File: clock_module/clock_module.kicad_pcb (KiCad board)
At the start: 2 copper layers, 100 x 100 mm, 19 parts, among them SW1 SW_SPST, SW2 SW_Push, SW3 SW_SPDT, SW4 SW_SPDT, U1 74HC14

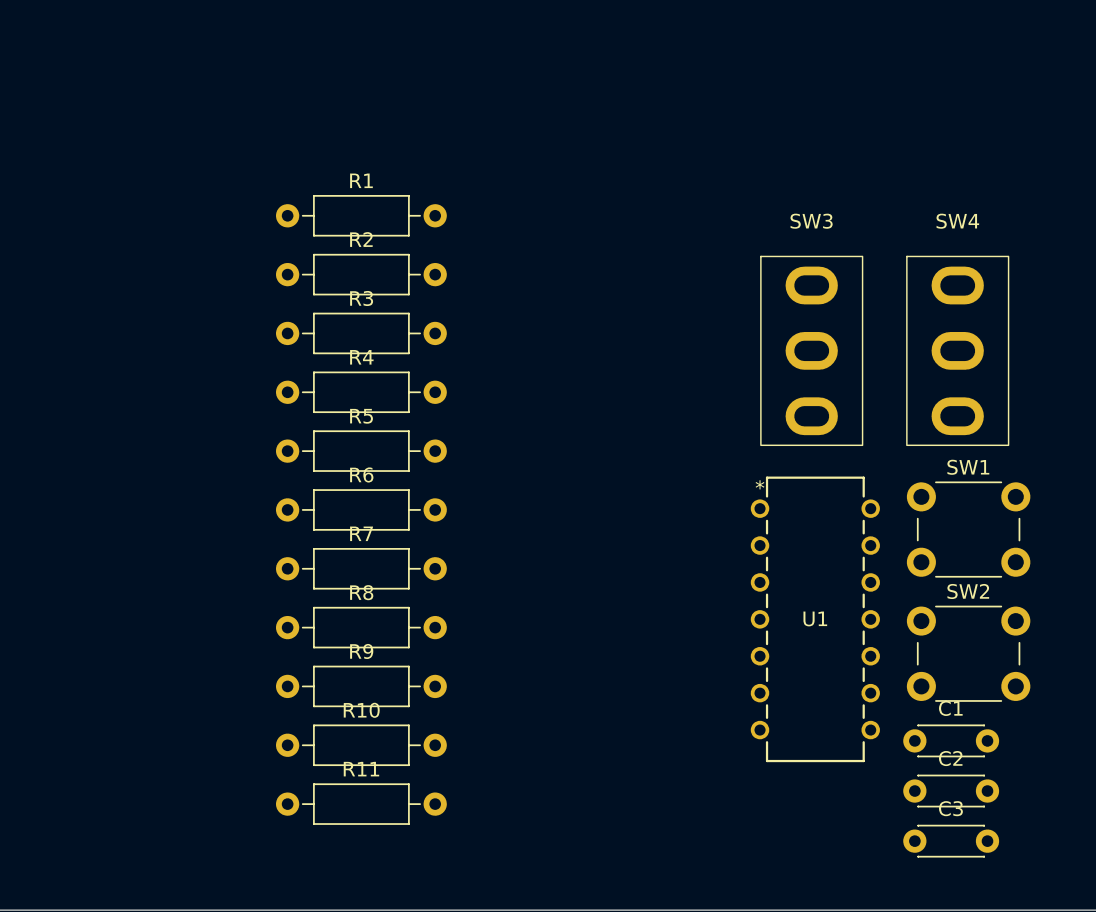
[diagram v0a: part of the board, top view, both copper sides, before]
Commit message: フットプリント追加
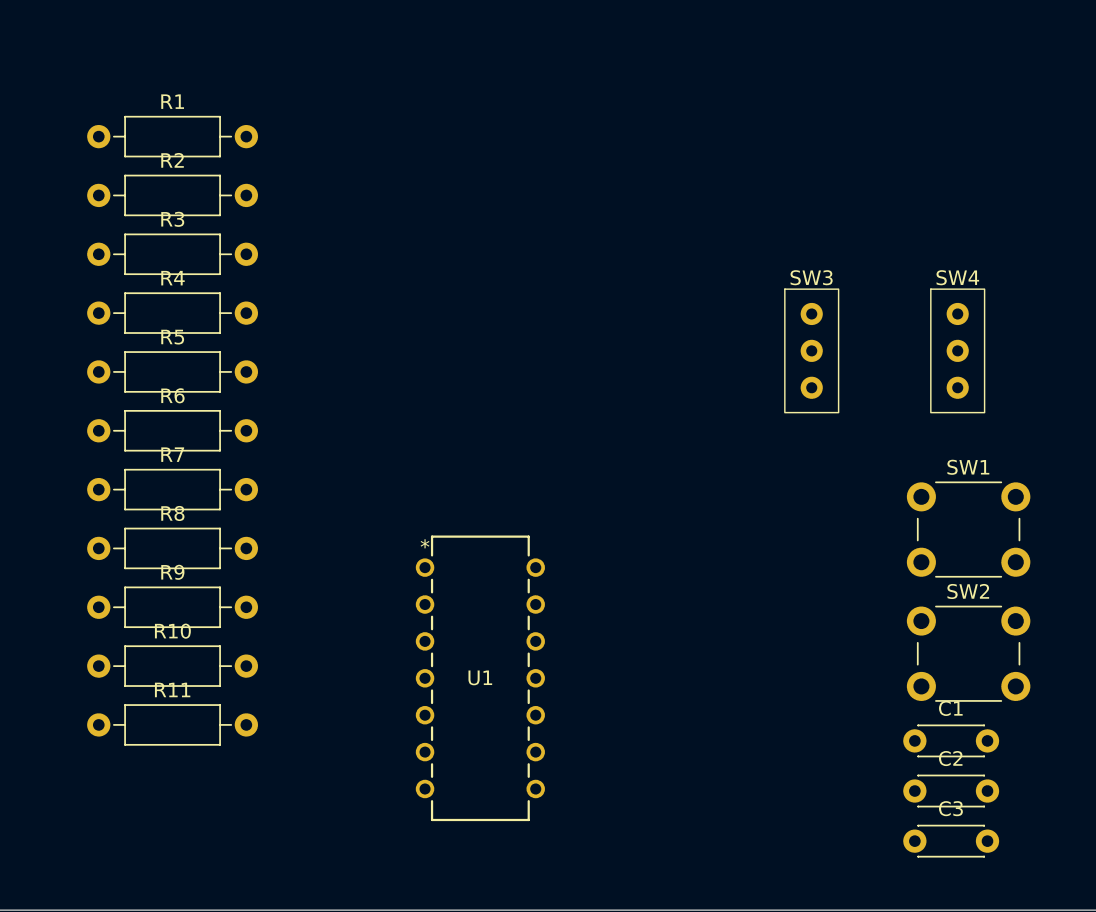
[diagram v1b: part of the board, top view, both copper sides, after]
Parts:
- SW3, SW4: footprint footprint_library:SPDT -> footprint_library:SS-12D00G3
- moved U1 23.4 mm to (136.4, 126.4)
- moved R10 14.1 mm to (113.9, 133.2)
- moved R8 14.1 mm to (113.9, 125.1)
- moved R1 14.1 mm to (113.9, 96.8)
- moved R2 14.1 mm to (113.9, 100.8)
- moved R3 14.1 mm to (113.9, 104.8)
- moved R5 14.1 mm to (113.9, 113.0)
- moved R6 14.1 mm to (113.9, 117.0)
- moved R7 14.1 mm to (113.9, 121.0)
- moved R11 14.1 mm to (113.9, 137.2)
- moved R4 14.1 mm to (113.9, 108.9)
- moved R9 14.1 mm to (113.9, 129.2)
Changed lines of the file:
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@@
 	(footprint "Resistor_THT:R_Axial_DIN0207_L6.3mm_D2.5mm_P10.16mm_Horizontal"
 		(layer "F.Cu")
-		(at 126.92 102.2)
+		(at 113.92 96.75)
 		(descr "Resistor, Axial_DIN0207 series, Axial, Horizontal, pin pitch=10.16mm, 0.25W = 1/4W, length*diameter=6.3*2.5mm^2, http://cdn-reichelt.de/documents/datenblatt/B400/1_4W%23YAG.pdf")
 		(tags "Resistor Axial_DIN0207 series Axial Horizontal pin pitch 10.16mm 0.25W = 1/4W length 6.3mm diameter 2.5mm")
@@
 	(footprint "Resistor_THT:R_Axial_DIN0207_L6.3mm_D2.5mm_P10.16mm_Horizontal"
 		(layer "F.Cu")
-		(at 126.92 122.45)
+		(at 113.92 117)
 		(descr "Resistor, Axial_DIN0207 series, Axial, Horizontal, pin pitch=10.16mm, 0.25W = 1/4W, length*diameter=6.3*2.5mm^2, http://cdn-reichelt.de/documents/datenblatt/B400/1_4W%23YAG.pdf")
 		(tags "Resistor Axial_DIN0207 series Axial Horizontal pin pitch 10.16mm 0.25W = 1/4W length 6.3mm diameter 2.5mm")
@@
 	(footprint "Resistor_THT:R_Axial_DIN0207_L6.3mm_D2.5mm_P10.16mm_Horizontal"
 		(layer "F.Cu")
-		(at 126.92 110.3)
+		(at 113.92 104.85)
 		(descr "Resistor, Axial_DIN0207 series, Axial, Horizontal, pin pitch=10.16mm, 0.25W = 1/4W, length*diameter=6.3*2.5mm^2, http://cdn-reichelt.de/documents/datenblatt/B400/1_4W%23YAG.pdf")
 		(tags "Resistor Axial_DIN0207 series Axial Horizontal pin pitch 10.16mm 0.25W = 1/4W length 6.3mm diameter 2.5mm")
@@
 		)
 	)
-	(footprint "footprint_library:SPDT"
+	(footprint "footprint_library:SS-12D00G3"
 		(layer "F.Cu")
 		(at 173.05 111.5)
 		(property "Reference" "SW4"
-			(at 0 -8.89 0)
+			(at 0 -5 0)
 			(unlocked yes)
 			(layer "F.SilkS")
@@
 		)
 		(property "Value" "SW_SPDT"
-			(at 0 -7.62 0)
+			(at 0 1 0)
 			(unlocked yes)
 			(layer "F.Fab")
@@
 			)
 		)
-		(property "Footprint" "footprint_library:SPDT"
+		(property "Footprint" "footprint_library:SS-12D00G3"
 			(at 0 0 0)
+			(unlocked yes)
 			(layer "F.Fab")
 			(hide yes)
 			(effects
 				(font
-					(size 1.27 1.27)
+					(size 1 1)
 					(thickness 0.15)
 				)
@@
 		(property "Datasheet" ""
 			(at 0 0 0)
+			(unlocked yes)
 			(layer "F.Fab")
 			(hide yes)
 			(effects
 				(font
-					(size 1.27 1.27)
+					(size 1 1)
 					(thickness 0.15)
 				)
@@
 		(property "Description" "Switch, single pole double throw"
 			(at 0 0 0)
+			(unlocked yes)
 			(layer "F.Fab")
 			(hide yes)
 			(effects
 				(font
-					(size 1.27 1.27)
+					(size 1 1)
 					(thickness 0.15)
 				)
@@
 		(attr through_hole)
 		(fp_rect
-			(start -3.5 -6.5)
-			(end 3.5 6.5)
+			(start -1.85 -4.25)
+			(end 1.85 4.25)
 			(stroke
 				(width 0.1)
@@
 		)
 		(fp_rect
-			(start -4.5 -7.5)
-			(end 4.5 7.5)
+			(start -2.54 -5.08)
+			(end 2.54 5.08)
 			(stroke
 				(width 0.05)
@@
 		)
 		(fp_text user "${REFERENCE}"
-			(at 0 -1.31 0)
+			(at 0 2.5 0)
 			(unlocked yes)
 			(layer "F.Fab")
@@
 			)
 		)
-		(pad "1" thru_hole oval
-			(at 0 -4.5)
-			(size 3.6 2.6)
-			(drill oval 2.4 1.4)
+		(pad "1" thru_hole circle
+			(at 0 -2.54)
+			(size 1.524 1.524)
+			(drill 0.762)
 			(layers "*.Cu" "*.Mask")
 			(remove_unused_layers no)
@@
 			(pintype "passive")
 		)
-		(pad "2" thru_hole oval
+		(pad "2" thru_hole circle
 			(at 0 0)
-			(size 3.6 2.6)
-			(drill oval 2.4 1.4)
+			(size 1.524 1.524)
+			(drill 0.762)
 			(layers "*.Cu" "*.Mask")
 			(remove_unused_layers no)
@@
 			(pintype "passive")
 		)
-		(pad "3" thru_hole oval
-			(at 0 4.5)
-			(size 3.6 2.6)
-			(drill oval 2.4 1.4)
+		(pad "3" thru_hole circle
+			(at 0 2.54)
+			(size 1.524 1.524)
+			(drill 0.762)
 			(layers "*.Cu" "*.Mask")
 			(remove_unused_layers no)
@@
 	(footprint "Resistor_THT:R_Axial_DIN0207_L6.3mm_D2.5mm_P10.16mm_Horizontal"
 		(layer "F.Cu")
-		(at 126.92 134.6)
+		(at 113.92 129.15)
 		(descr "Resistor, Axial_DIN0207 series, Axial, Horizontal, pin pitch=10.16mm, 0.25W = 1/4W, length*diameter=6.3*2.5mm^2, http://cdn-reichelt.de/documents/datenblatt/B400/1_4W%23YAG.pdf")
 		(tags "Resistor Axial_DIN0207 series Axial Horizontal pin pitch 10.16mm 0.25W = 1/4W length 6.3mm diameter 2.5mm")
@@
 	(footprint "Resistor_THT:R_Axial_DIN0207_L6.3mm_D2.5mm_P10.16mm_Horizontal"
 		(layer "F.Cu")
-		(at 126.92 118.4)
+		(at 113.92 112.95)
 		(descr "Resistor, Axial_DIN0207 series, Axial, Horizontal, pin pitch=10.16mm, 0.25W = 1/4W, length*diameter=6.3*2.5mm^2, http://cdn-reichelt.de/documents/datenblatt/B400/1_4W%23YAG.pdf")
 		(tags "Resistor Axial_DIN0207 series Axial Horizontal pin pitch 10.16mm 0.25W = 1/4W length 6.3mm diameter 2.5mm")
@@
 	(footprint "Resistor_THT:R_Axial_DIN0207_L6.3mm_D2.5mm_P10.16mm_Horizontal"
 		(layer "F.Cu")
-		(at 126.92 138.65)
+		(at 113.92 133.2)
 		(descr "Resistor, Axial_DIN0207 series, Axial, Horizontal, pin pitch=10.16mm, 0.25W = 1/4W, length*diameter=6.3*2.5mm^2, http://cdn-reichelt.de/documents/datenblatt/B400/1_4W%23YAG.pdf")
 		(tags "Resistor Axial_DIN0207 series Axial Horizontal pin pitch 10.16mm 0.25W = 1/4W length 6.3mm diameter 2.5mm")
@@
 	(footprint "footprint_library:DIP14_TOS"
 		(layer "F.Cu")
-		(at 159.4402 122.3618)
+		(at 136.38 126.42)
 		(tags "tc74hc14apf ")
 		(property "Reference" "U1"
@@
 	(footprint "Resistor_THT:R_Axial_DIN0207_L6.3mm_D2.5mm_P10.16mm_Horizontal"
 		(layer "F.Cu")
-		(at 126.92 142.7)
+		(at 113.92 137.25)
 		(descr "Resistor, Axial_DIN0207 series, Axial, Horizontal, pin pitch=10.16mm, 0.25W = 1/4W, length*diameter=6.3*2.5mm^2, http://cdn-reichelt.de/documents/datenblatt/B400/1_4W%23YAG.pdf")
 		(tags "Resistor Axial_DIN0207 series Axial Horizontal pin pitch 10.16mm 0.25W = 1/4W length 6.3mm diameter 2.5mm")
@@
 	(footprint "Resistor_THT:R_Axial_DIN0207_L6.3mm_D2.5mm_P10.16mm_Horizontal"
 		(layer "F.Cu")
-		(at 126.92 106.25)
+		(at 113.92 100.8)
 		(descr "Resistor, Axial_DIN0207 series, Axial, Horizontal, pin pitch=10.16mm, 0.25W = 1/4W, length*diameter=6.3*2.5mm^2, http://cdn-reichelt.de/documents/datenblatt/B400/1_4W%23YAG.pdf")
 		(tags "Resistor Axial_DIN0207 series Axial Horizontal pin pitch 10.16mm 0.25W = 1/4W length 6.3mm diameter 2.5mm")
@@
 	(footprint "Resistor_THT:R_Axial_DIN0207_L6.3mm_D2.5mm_P10.16mm_Horizontal"
 		(layer "F.Cu")
-		(at 126.92 130.55)
+		(at 113.92 125.1)
 		(descr "Resistor, Axial_DIN0207 series, Axial, Horizontal, pin pitch=10.16mm, 0.25W = 1/4W, length*diameter=6.3*2.5mm^2, http://cdn-reichelt.de/documents/datenblatt/B400/1_4W%23YAG.pdf")
 		(tags "Resistor Axial_DIN0207 series Axial Horizontal pin pitch 10.16mm 0.25W = 1/4W length 6.3mm diameter 2.5mm")
@@
 		)
 	)
-	(footprint "footprint_library:SPDT"
+	(footprint "footprint_library:SS-12D00G3"
 		(layer "F.Cu")
 		(at 163 111.5)
 		(property "Reference" "SW3"
-			(at 0 -8.89 0)
+			(at 0 -5 0)
 			(unlocked yes)
 			(layer "F.SilkS")
@@
 		)
 		(property "Value" "SW_SPDT"
-			(at 0 -7.62 0)
+			(at 0 1 0)
 			(unlocked yes)
 			(layer "F.Fab")
@@
 			)
 		)
-		(property "Footprint" "footprint_library:SPDT"
+		(property "Footprint" "footprint_library:SS-12D00G3"
 			(at 0 0 0)
+			(unlocked yes)
 			(layer "F.Fab")
 			(hide yes)
 			(effects
 				(font
-					(size 1.27 1.27)
+					(size 1 1)
 					(thickness 0.15)
 				)
@@
 		(property "Datasheet" ""
 			(at 0 0 0)
+			(unlocked yes)
 			(layer "F.Fab")
 			(hide yes)
 			(effects
 				(font
-					(size 1.27 1.27)
+					(size 1 1)
 					(thickness 0.15)
 				)
@@
 		(property "Description" "Switch, single pole double throw"
 			(at 0 0 0)
+			(unlocked yes)
 			(layer "F.Fab")
 			(hide yes)
 			(effects
 				(font
-					(size 1.27 1.27)
+					(size 1 1)
 					(thickness 0.15)
 				)
@@
 		(attr through_hole)
 		(fp_rect
-			(start -3.5 -6.5)
-			(end 3.5 6.5)
+			(start -1.85 -4.25)
+			(end 1.85 4.25)
 			(stroke
 				(width 0.1)
@@
 		)
 		(fp_rect
-			(start -4.5 -7.5)
-			(end 4.5 7.5)
+			(start -2.54 -5.08)
+			(end 2.54 5.08)
 			(stroke
 				(width 0.05)
@@
 		)
 		(fp_text user "${REFERENCE}"
-			(at 0 -1.31 0)
+			(at 0 2.5 0)
 			(unlocked yes)
 			(layer "F.Fab")
@@
 			)
 		)
-		(pad "1" thru_hole oval
-			(at 0 -4.5)
-			(size 3.6 2.6)
-			(drill oval 2.4 1.4)
+		(pad "1" thru_hole circle
+			(at 0 -2.54)
+			(size 1.524 1.524)
+			(drill 0.762)
 			(layers "*.Cu" "*.Mask")
 			(remove_unused_layers no)
@@
 			(pintype "passive")
 		)
-		(pad "2" thru_hole oval
+		(pad "2" thru_hole circle
 			(at 0 0)
-			(size 3.6 2.6)
-			(drill oval 2.4 1.4)
+			(size 1.524 1.524)
+			(drill 0.762)
 			(layers "*.Cu" "*.Mask")
 			(remove_unused_layers no)
@@
 			(pintype "passive")
 		)
-		(pad "3" thru_hole oval
-			(at 0 4.5)
-			(size 3.6 2.6)
-			(drill oval 2.4 1.4)
+		(pad "3" thru_hole circle
+			(at 0 2.54)
+			(size 1.524 1.524)
+			(drill 0.762)
 			(layers "*.Cu" "*.Mask")
 			(remove_unused_layers no)
@@
 	(footprint "Resistor_THT:R_Axial_DIN0207_L6.3mm_D2.5mm_P10.16mm_Horizontal"
 		(layer "F.Cu")
-		(at 126.92 126.5)
+		(at 113.92 121.05)
 		(descr "Resistor, Axial_DIN0207 series, Axial, Horizontal, pin pitch=10.16mm, 0.25W = 1/4W, length*diameter=6.3*2.5mm^2, http://cdn-reichelt.de/documents/datenblatt/B400/1_4W%23YAG.pdf")
 		(tags "Resistor Axial_DIN0207 series Axial Horizontal pin pitch 10.16mm 0.25W = 1/4W length 6.3mm diameter 2.5mm")
@@
 	(footprint "Resistor_THT:R_Axial_DIN0207_L6.3mm_D2.5mm_P10.16mm_Horizontal"
 		(layer "F.Cu")
-		(at 126.92 114.35)
+		(at 113.92 108.9)
 		(descr "Resistor, Axial_DIN0207 series, Axial, Horizontal, pin pitch=10.16mm, 0.25W = 1/4W, length*diameter=6.3*2.5mm^2, http://cdn-reichelt.de/documents/datenblatt/B400/1_4W%23YAG.pdf")
 		(tags "Resistor Axial_DIN0207 series Axial Horizontal pin pitch 10.16mm 0.25W = 1/4W length 6.3mm diameter 2.5mm")

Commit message: 電源回路wip
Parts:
- added C1: 100uF, Capacitor_THT:C_Disc_D4.3mm_W1.9mm_P5.00mm, F.Cu at (130.8, 78.1)
- added C10: 0.1uF, Capacitor_THT:C_Disc_D4.3mm_W1.9mm_P5.00mm, F.Cu at (139.7, 85.7)
- added C11: 0.1uF, Capacitor_THT:C_Disc_D4.3mm_W1.9mm_P5.00mm, F.Cu at (144.1, 85.7)
- added C12: 0.1uF, Capacitor_THT:C_Disc_D4.3mm_W1.9mm_P5.00mm, F.Cu at (148.6, 85.7)
- added C13: 0.1uF, Capacitor_THT:C_Disc_D4.3mm_W1.9mm_P5.00mm, F.Cu at (153.0, 85.7)
- added C14: 0.1uF, Capacitor_THT:C_Disc_D4.3mm_W1.9mm_P5.00mm, F.Cu at (157.5, 85.7)
- added C2: 0.1uF, Capacitor_THT:C_Disc_D4.3mm_W1.9mm_P5.00mm, F.Cu at (135.3, 78.1)
- added C3: 0.1uF, Capacitor_THT:C_Disc_D4.3mm_W1.9mm_P5.00mm, F.Cu at (139.7, 78.1)
- added C4: 0.1uF, Capacitor_THT:C_Disc_D4.3mm_W1.9mm_P5.00mm, F.Cu at (144.1, 78.1)
- added C5: 0.1uF, Capacitor_THT:C_Disc_D4.3mm_W1.9mm_P5.00mm, F.Cu at (148.6, 78.1)
- added C6: 0.1uF, Capacitor_THT:C_Disc_D4.3mm_W1.9mm_P5.00mm, F.Cu at (153.0, 78.1)
- added C7: 0.1uF, Capacitor_THT:C_Disc_D4.3mm_W1.9mm_P5.00mm, F.Cu at (157.5, 78.1)
- added C8: 0.1uF, Capacitor_THT:C_Disc_D4.3mm_W1.9mm_P5.00mm, F.Cu at (130.8, 85.7)
- added C9: 0.1uF, Capacitor_THT:C_Disc_D4.3mm_W1.9mm_P5.00mm, F.Cu at (135.3, 85.7)
- added J1: USB_C_Receptacle_PowerOnly_6P, footprint_library:UJC-HP-3-SMT-TR, F.Cu at (103.5, 77.2)
- added J2: Conn_01x02_Socket, Connector_PinSocket_2.54mm:PinSocket_1x02_P2.54mm_Horizontal, F.Cu at (188.6, 73.7)
- added R1: 1K, Resistor_THT:R_Axial_DIN0207_L6.3mm_D2.5mm_P10.16mm_Horizontal, F.Cu at (124.5, 83.2)
- added R2: 5.1K, Resistor_THT:R_Axial_DIN0207_L6.3mm_D2.5mm_P10.16mm_Horizontal, F.Cu at (114.3, 83.2)
- added R3: 5.1K, Resistor_THT:R_Axial_DIN0207_L6.3mm_D2.5mm_P10.16mm_Horizontal, F.Cu at (119.4, 83.2)
- moved SW1 34.7 mm to (140.9, 112.0)
- moved SW4 18.2 mm to (152.3, 122.2)
- moved C15 9.07 mm to (174.0, 133.6)
- moved C16 9.07 mm to (174.0, 137.1)
- moved C17 9.07 mm to (174.0, 130.2)
- renumbered C2 to C15, C3 to C16, C1 to C17, R7 to R10, R1 to R12, R2 to R13, R3 to R14, R8 to R7, R9 to R8, R10 to R9, SW2 to SW1, SW4 to SW2, SW1 to SW4

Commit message: 位置調整wip
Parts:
- moved R14 65.5 mm to (177.8, 119.4)
- moved SW2 52.7 mm to (122.6, 96.5)
- moved SW3 49.6 mm to (115.9, 96.1)
- moved C15 49.3 mm to (144.9, 93.9)
- moved C16 49.3 mm to (144.9, 97.4)
- moved R13 49.1 mm to (159.4, 119.4)
- moved R12 39.7 mm to (152.4, 106.7), turned to -90 degrees
- moved SW1 22.4 mm to (131.4, 91.7)
- moved U1 19.0 mm to (128.3, 109.2)
- moved R4 9.58 mm to (104.8, 106.0)
- moved R5 9.25 mm to (105.0, 110.4)
- moved R6 9.25 mm to (105.0, 114.5)
- moved R8 9.25 mm to (105.0, 126.6)
- moved R10 9.25 mm to (105.0, 118.5)
- moved R11 9.25 mm to (105.0, 134.7)
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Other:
- board text added: "CLOCK"
- board text added: "RESET"
